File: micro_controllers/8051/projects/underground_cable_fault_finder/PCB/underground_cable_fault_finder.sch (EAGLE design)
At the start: 0 parts

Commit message: 
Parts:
- added AVRCONNECTOR, SL8: (no value), con-amp-quick:M05
- added BRIDGE: LM399H, linear:LM399H
- added C1, C2: 33pf, rcl:C-EU025-024X044
- added C3: 470uf, capacitor-wima:C5/7.2
- added C4: .01uf, capacitor-wima:C2,5-3
- added C5: 4.7uf, capacitor-wima:C2,5-3
- added C6: 0.1uf, capacitor-wima:C2.5/6
- added C7: 150pf, capacitor-wima:C2,5-3
- added CONN-6, CONN-7: 3 pin, con-amp-quick:M03
- added CONNECTOR: LCD, con-amp-quick:M16
- added CONNECTOR-5: 4 pin, con-amp-quick:M04
- added CRYSTAL: 11.0592 mhz, special:XTAL/S
- added D1, D2, D3: 1N4007, diode:1N4004
- added IC1: AT89S51, atmel:AT89C51-12PC
- added IC2: 7805TV, linear:7805TV
- added IC3: adc804, atmel:ATF16V8BP3
- added J1: (no value), con-jack:JACK-PLUG0
- added JP1: TRANSFORMER, jumper:JP1Q
- added LED2: 5mm, led:LED5MM
- added LED3, LED4, LED5: 5MM, led:LED5MM
- added R1, R10, R11, R12, R13, R14, R15, R3, R4, R5, R6, R7, R8, R9: 10k, eagle-ltspice:R0204/7
- added R16, R17, R21: 1K, rcl:R-EU_0204/7
- added R18, R19, R20: 5.6K, rcl:R-EU_0204/7
- added R2: 560E, eagle-ltspice:R0204/7
- added RELAY-1, RELAY-2, RELAY-3: 12V, relay:G5L
- added RN10: 10 k, con-amp-quick:M09
- added S1: ON/ OFF SWITCH, switch-dil:DA03
- added S10, S11, S12, S13, S14, S3, S4, S5, S6, S7, S8, S9: (no value), switch:255SB
- added S2: push switch, switch-dil:DP02
- added SL2: (no value), con-amp-quick:M02
- added SL3: LM35, con-amp-quick:M03
- added T1, T2, T3: BC547, transistor:BC547
- added VR, VR1: 10k, resistor:R-TRIMM64P
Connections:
- new net N$1: C2.1, CRYSTAL.1, IC1.XTAL2
- new net N$10: IC1.P1.4, IC3.O6
- new net N$11: AVRCONNECTOR.5, IC1.P1.5, IC3.O7
- new net N$12: AVRCONNECTOR.1, IC1.P1.6, IC3.O8
- new net N$13: IC3.OE
- new net N$14: AVRCONNECTOR.3, C6.1, IC1.RST, R1.1, S2.1
- new net N$15: C5.1, C6.2, CONN-7.1, CONN-7.2, CONN-7.3, CONNECTOR-5.4, CONNECTOR.15, CONNECTOR.2, IC1.!EA!/VPP, IC1.VCC, IC2.VO, IC3.VCC, RN10.1, S2.2, SL2.1, SL3.1, SL8.2, SL8.3, SL8.4, SL8.5, VR.E, VR1.E
- new net N$16: BRIDGE.4, J1.1, J1.2, JP1.1
- new net N$17: IC3.O1, R3.2
- new net N$18: C7.1, IC3.I3, R3.1
- new net N$19: IC3.I5, SL3.2
- new net N$2: C1.1, CRYSTAL.2, IC1.XTAL1
- new net N$20: S10.S, S11.S, S12.S, S13.S, S14.S, S3.S, S4.S, S5.S, S6.S, S7.S, S8.S, S9.S
- new net N$21: R4.2, S8.P
- new net N$22: R5.2, S3.P
- new net N$23: IC3.I8, VR1.S
- new net N$24: IC1.P0.2_AD2, RN10.4
- new net N$25: IC1.P0.3_AD3, R18.2, RN10.5
- new net N$27: IC1.P0.5_AD5, RN10.7
- new net N$28: IC1.P0.6_AD6, RN10.8
- new net N$29: IC1.P0.7_AD7, RN10.9
- new net N$3: BRIDGE.1, C1.2, C2.2, C3.1, C4.2, C5.2, C7.2, CONNECTOR-5.1, CONNECTOR-5.2, CONNECTOR.1, CONNECTOR.16, CONNECTOR.5, IC1.GND, IC2.GND, IC3.CLK, IC3.GND, IC3.I1, IC3.I6, IC3.I7, LED2.C, R1.2, RELAY-12.S, RELAY-22.S, RELAY-32.S, S10.O, S14.O, S5.O, SL2.2, SL3.3, SL8.1, T1.E, T2.E, T3.E, VR.A, VR1.A
- new net N$30: CONNECTOR.7, IC1.P2.0_A8
- new net N$31: CONNECTOR.8, IC1.P2.1_A9
- new net N$32: CONNECTOR.9, IC1.P2.2_A10
- new net N$33: R5.1, S8.O
- new net N$34: R6.2, S4.P
- new net N$35: CONNECTOR.12, IC1.P2.5_A13
- new net N$36: R6.1, S3.O
- new net N$37: R7.2, S5.P
- new net N$38: CONNECTOR.3, VR.S
- new net N$4: C3.2, C4.1, CONN-6.1, CONN-6.2, CONN-6.3, CONNECTOR-5.3, D1.C, D2.C, D3.C, IC2.VI, R16.2, R17.2, R2.2, R21.1, RELAY-11.1, RELAY-21.1, RELAY-31.1, S1.5
- new net N$40: R9.1, S9.O
- new net N$41: R8.2, S9.P
- new net N$42: R9.2, S6.P
- new net N$43: LED2.A, R2.1
- new net N$44: R10.1, S6.O
- new net N$45: AVRCONNECTOR.2, IC1.P1.7
- new net N$47: BRIDGE.3, S1.6
- new net N$48: CONNECTOR.6, IC1.P0.1_AD1, RN10.3
- new net N$49: S7.P
- new net N$5: BRIDGE.2, J1.3, JP1.2
- new net N$50: R11.1, S7.O
- new net N$51: CONNECTOR.10, IC1.P2.3_A11
- new net N$52: CONNECTOR.11, IC1.P2.4_A12
- new net N$53: S10.P
- new net N$54: CONNECTOR.13, IC1.P2.6_A14
- new net N$55: CONNECTOR.14, IC1.P2.7_A15
- new net N$57: R12.2, S11.P
- new net N$58: CONNECTOR.4, IC1.P0.0_AD0, RN10.2
- new net N$59: R13.2, S12.P
- new net N$6: IC1.P1.0, IC3.O2
- new net N$60: R14.2, S13.P
- new net N$61: S14.P
- new net N$62: R13.1, S11.O
- new net N$63: R14.1, S12.O
- new net N$64: R15.1, S13.O
- new net N$65: D1.A, LED3.C, RELAY-11.2, T2.C
- new net N$67: R19.1, T1.B
- new net N$68: R18.1, T2.B
- new net N$69: LED3.A, R17.1
- new net N$7: IC1.P1.1, IC3.O3
- new net N$70: LED4.A, R16.1
- new net N$72: R8.1, RELAY-12.P
- new net N$73: R12.1, RELAY-22.P
- new net N$74: R20.2
- new net N$75: D2.A, LED4.C, RELAY-21.2, T1.C
- new net N$77: D3.A, LED5.C, RELAY-31.2, T3.C
- new net N$78: R20.1, T3.B
- new net N$79: LED5.A, R21.2
- new net N$8: IC1.P1.2, IC3.O4
- new net N$80: R4.1, RELAY-32.P
- new net N$83: IC1.P0.4_AD4, R19.2, RN10.6
- new net N$84: R7.1, S4.O
- new net N$9: IC1.P1.3, IC3.O5

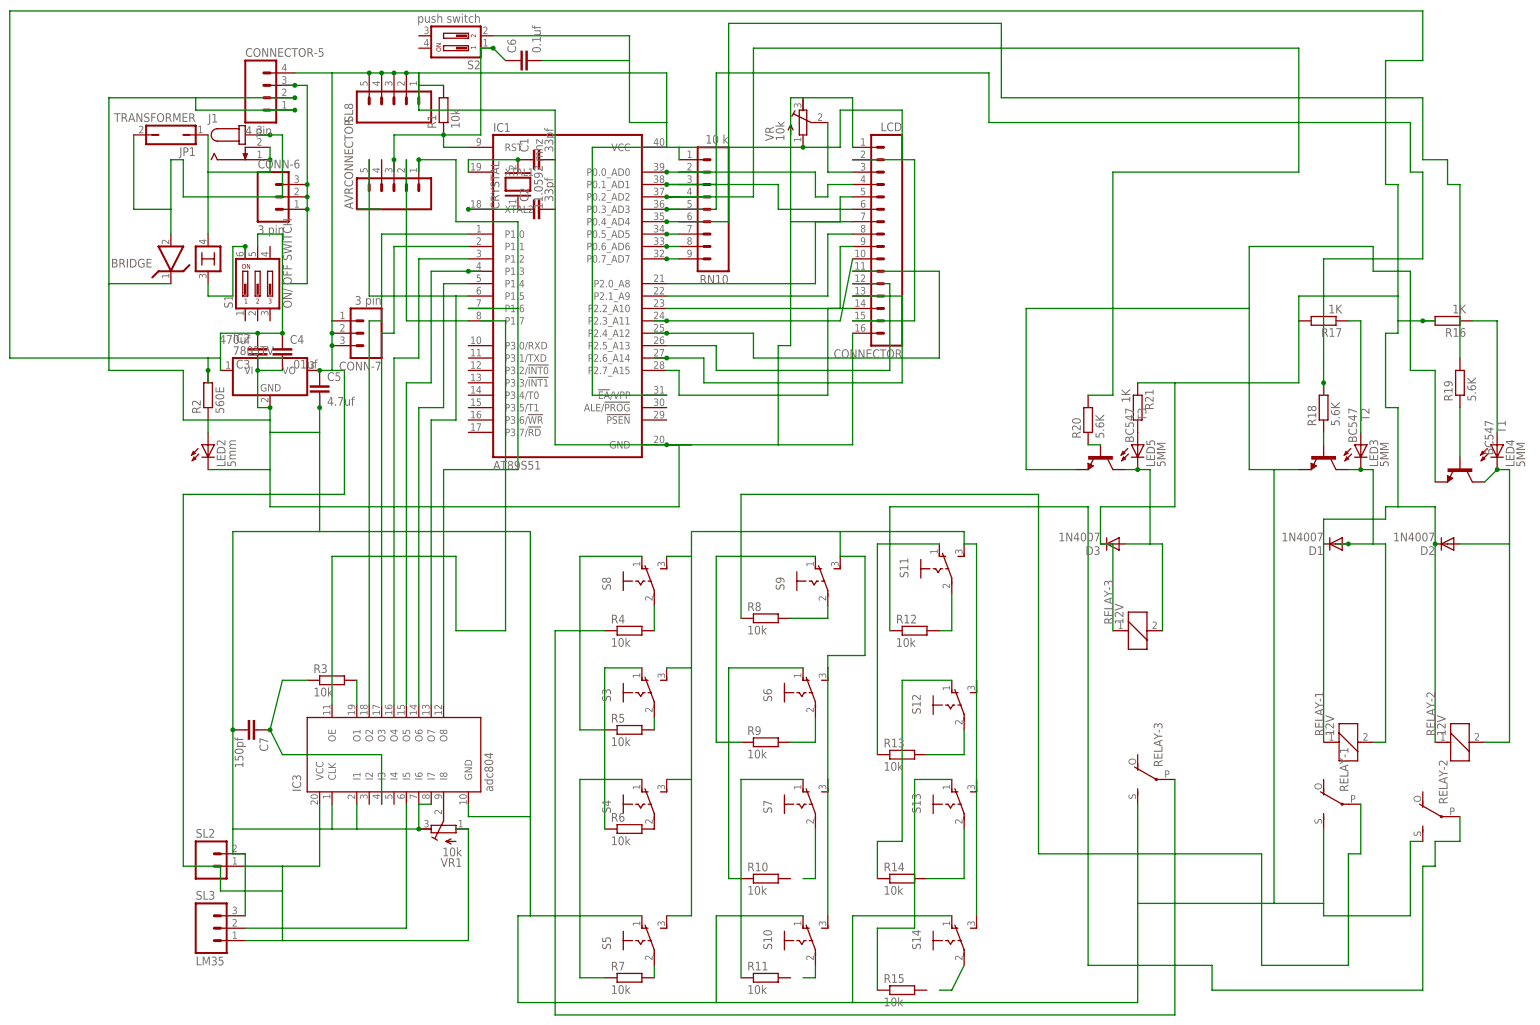
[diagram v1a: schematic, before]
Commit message: 
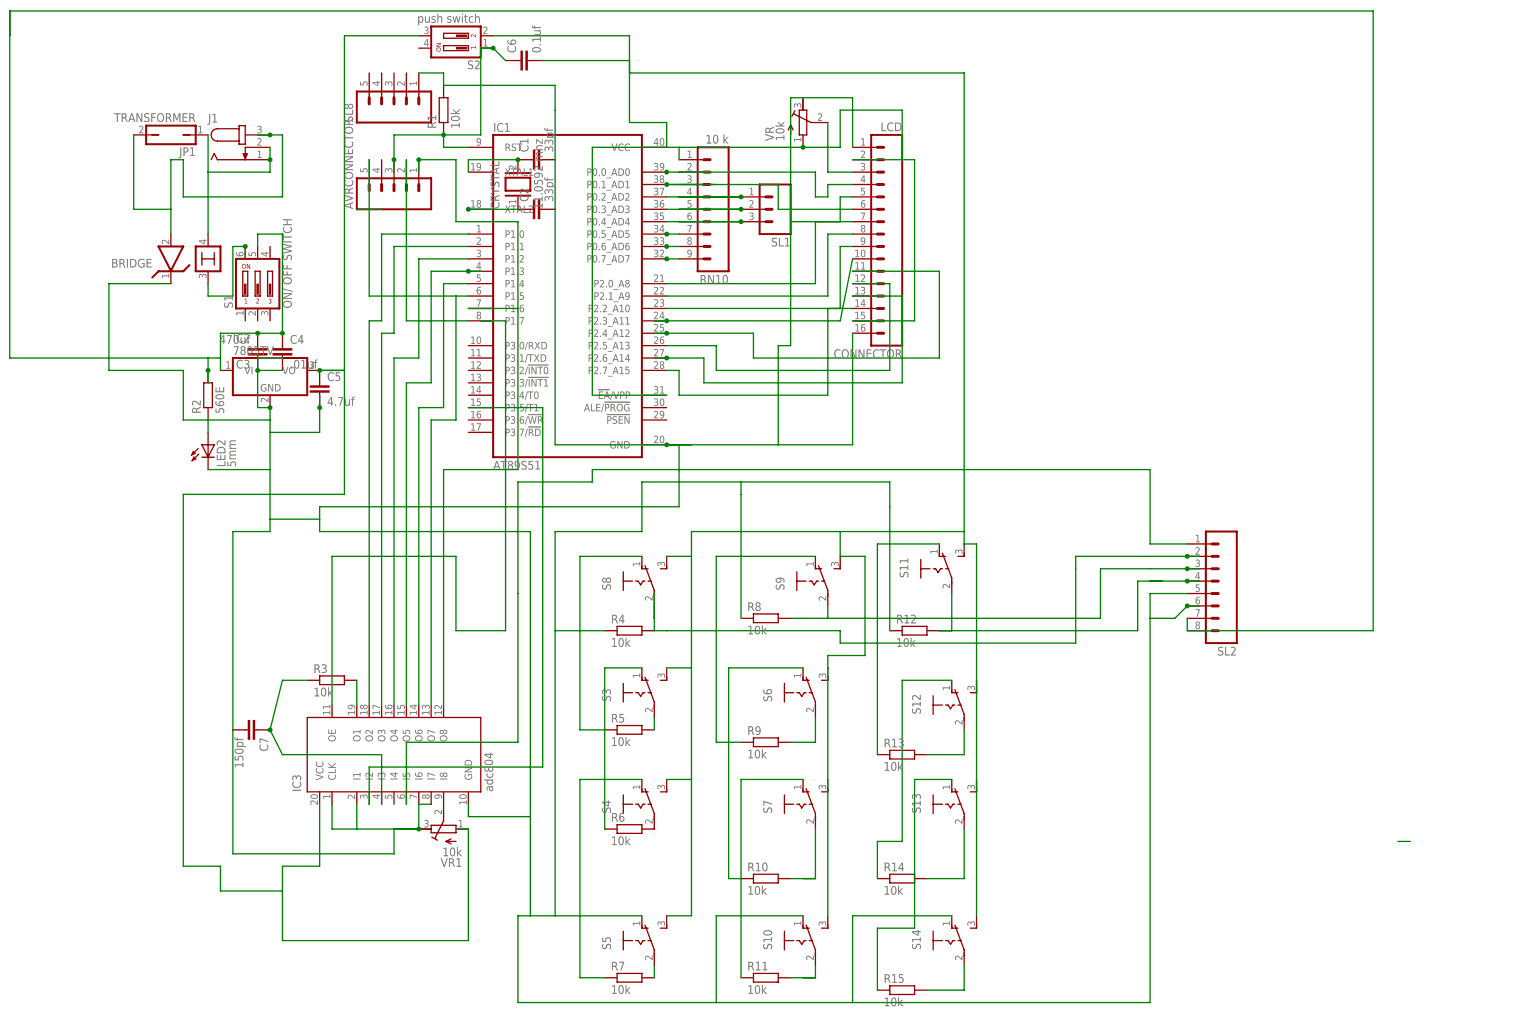
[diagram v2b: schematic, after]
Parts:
- removed CONN-6, CONN-7: 3 pin, con-amp-quick:M03
- removed CONNECTOR-5: 4 pin, con-amp-quick:M04
- removed D1, D2, D3: 1N4007, diode:1N4004
- removed LED3, LED4, LED5: 5MM, led:LED5MM
- removed R16, R17, R21: 1K, rcl:R-EU_0204/7
- removed R18, R19, R20: 5.6K, rcl:R-EU_0204/7
- removed RELAY-1, RELAY-2, RELAY-3: 12V, relay:G5L
- removed SL3: LM35, con-amp-quick:M03
- removed T1, T2, T3: BC547, transistor:BC547
- added SL1: (no value), con-amp-quick:M03
- SL2: device con-amp-quick:M02 -> con-amp-quick:M08
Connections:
- removed net N$15: C5.1, C6.2, CONN-7.1, CONN-7.2, CONN-7.3, CONNECTOR-5.4, CONNECTOR.15, CONNECTOR.2, IC1.!EA!/VPP, IC1.VCC, IC2.VO, IC3.VCC, RN10.1, S2.2, SL2.1, SL3.1, SL8.2, SL8.3, SL8.4, SL8.5, VR.E, VR1.E
- removed net N$24: IC1.P0.2_AD2, RN10.4
- removed net N$4: C3.2, C4.1, CONN-6.1, CONN-6.2, CONN-6.3, CONNECTOR-5.3, D1.C, D2.C, D3.C, IC2.VI, R16.2, R17.2, R2.2, R21.1, RELAY-11.1, RELAY-21.1, RELAY-31.1, S1.5
- removed net N$41: R8.2, S9.P
- removed net N$65: D1.A, LED3.C, RELAY-11.2, T2.C
- removed net N$67: R19.1, T1.B
- removed net N$68: R18.1, T2.B
- removed net N$69: LED3.A, R17.1
- removed net N$70: LED4.A, R16.1
- removed net N$72: R8.1, RELAY-12.P
- removed net N$73: R12.1, RELAY-22.P
- removed net N$75: D2.A, LED4.C, RELAY-21.2, T1.C
- removed net N$77: D3.A, LED5.C, RELAY-31.2, T3.C
- removed net N$78: R20.1, T3.B
- removed net N$79: LED5.A, R21.2
- removed net N$80: R4.1, RELAY-32.P
- new net N$26: IC1.P3.5/T1, IC3.I2
- new net N$39: IC3.I5, SL2.1
- new net N$71: C3.2, C4.1, IC2.VI, R2.2, S1.5, SL2.7, SL2.8
- new net N$76: R12.2, S11.P, SL2.4
- net N$19: now also R4.2, S8.P, SL2.2; no longer IC3.I5, SL3.2
- net N$20: now also C6.2, CONNECTOR.15, CONNECTOR.2, IC1.!EA!/VPP, IC1.VCC, RN10.1, S2.2, VR.E
- net N$21: now also R8.2, S9.P, SL2.3; no longer R4.2, S8.P
- net N$25: now also SL1.2; no longer R18.2
- net N$3: now also R12.1, R4.1, R8.1, SL2.5, SL2.6; no longer CONNECTOR-5.1, CONNECTOR-5.2, RELAY-12.S, RELAY-22.S, RELAY-32.S, SL2.2, SL3.3, T1.E, T2.E, T3.E
- net N$49: now also R10.2
- net N$53: now also R11.2
- net N$57: now also C5.1, IC2.VO, IC3.VCC, S2.3, VR1.E; no longer R12.2, S11.P
- net N$61: now also R15.2
- net N$74: now also IC1.P0.2_AD2, RN10.4, SL1.1; no longer R20.2
- net N$83: now also SL1.3; no longer R19.2

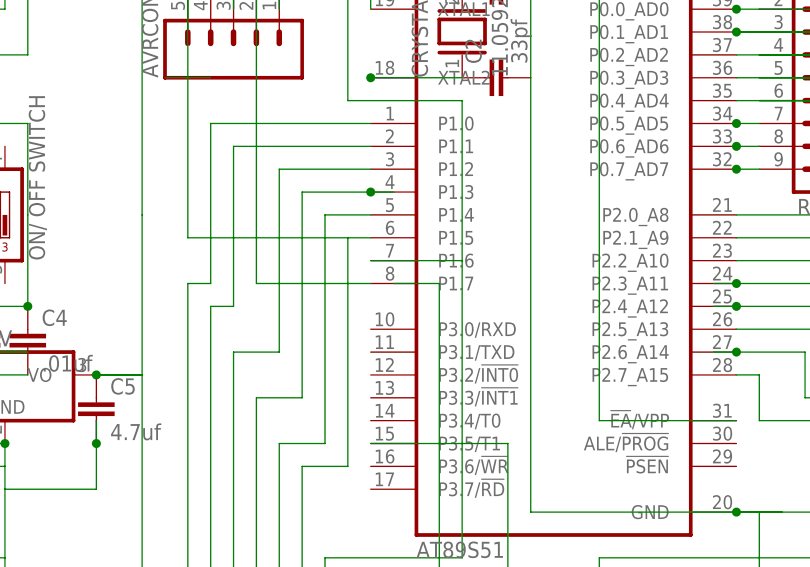
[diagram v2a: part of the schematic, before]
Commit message: 
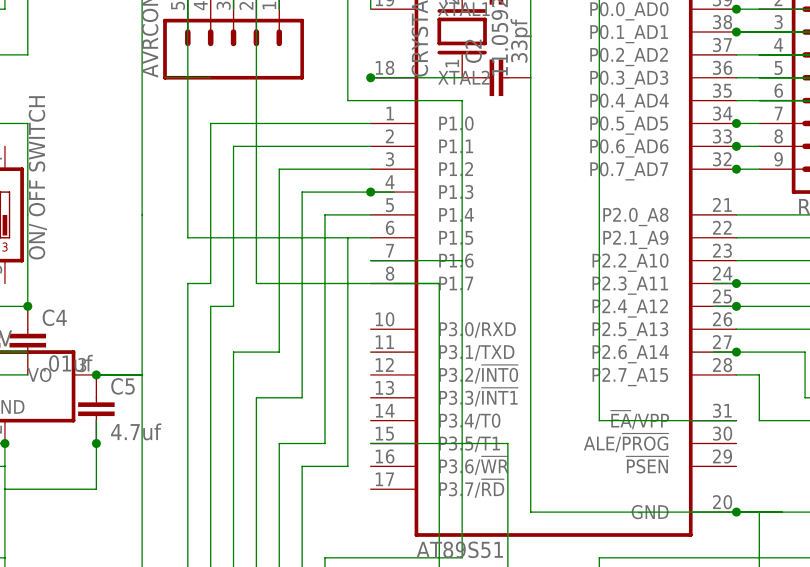
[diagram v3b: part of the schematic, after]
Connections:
- removed net N$13: IC3.OE
- net N$45: now also IC3.OE
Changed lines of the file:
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@@
 <?xml version="1.0" encoding="utf-8"?>
 <!DOCTYPE eagle SYSTEM "eagle.dtd">
-<eagle version="6.1">
+<eagle version="6.5.0">
 <drawing>
 <settings>
@@
 <wire x1="-12.7" y1="58.42" x2="-12.7" y2="91.44" width="0.1524" layer="91"/>
 <wire x1="-12.7" y1="58.42" x2="0" y2="58.42" width="0.1524" layer="91"/>
+<pinref part="IC3" gate="G$1" pin="OE"/>
+<wire x1="-27.94" y1="-20.32" x2="-27.94" y2="10.16" width="0.1524" layer="91"/>
+<wire x1="-27.94" y1="10.16" x2="-2.54" y2="10.16" width="0.1524" layer="91"/>
+<wire x1="-2.54" y1="10.16" x2="-2.54" y2="-5.08" width="0.1524" layer="91"/>
+<wire x1="-2.54" y1="-5.08" x2="7.62" y2="-5.08" width="0.1524" layer="91"/>
+<wire x1="7.62" y1="-5.08" x2="7.62" y2="58.42" width="0.1524" layer="91"/>
+<wire x1="7.62" y1="58.42" x2="2.54" y2="58.42" width="0.1524" layer="91"/>
+<wire x1="0" y1="58.42" x2="7.62" y2="58.42" width="0.1524" layer="91"/>
 </segment>
 </net>
@@
 </segment>
 </net>
-<net name="N$13" class="0">
-<segment>
-<pinref part="IC3" gate="G$1" pin="OE"/>
-<wire x1="-27.94" y1="-20.32" x2="-27.94" y2="10.16" width="0.1524" layer="91"/>
-<wire x1="-27.94" y1="10.16" x2="-2.54" y2="10.16" width="0.1524" layer="91"/>
-<wire x1="-2.54" y1="10.16" x2="-2.54" y2="-5.08" width="0.1524" layer="91"/>
-<wire x1="-2.54" y1="-5.08" x2="7.62" y2="-5.08" width="0.1524" layer="91"/>
-<wire x1="7.62" y1="-5.08" x2="7.62" y2="58.42" width="0.1524" layer="91"/>
-<wire x1="7.62" y1="58.42" x2="2.54" y2="58.42" width="0.1524" layer="91"/>
-</segment>
-</net>
